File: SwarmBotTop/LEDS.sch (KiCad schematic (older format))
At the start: 8 parts, among them IC2 PCA9532BS,118

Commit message: Camera routing with all sensors and motors
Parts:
- C21: value C -> 1uF
- IC2: symbol PCA9532BS_118:PCA9532BS,118 -> SwarmBot-rescue:PCA9532BS,118-PCA9532BS_118
- R17, R18, R19: value R -> 330R
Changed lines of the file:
@@
 $EndComp
 $Comp
-L PCA9532BS_118:PCA9532BS,118 IC2
+L SwarmBot-rescue:PCA9532BS,118-PCA9532BS_118 IC2
 U 1 1 5DED59B9
 P 1500 1900
+AR Path="/5DED59B9" Ref="IC2"  Part="1"
+AR Path="/5DAF9EB1/5DED0A15/5DED59B9" Ref="IC2"  Part="1"
 F 0 "IC2" H 3150 1550 50  0000 L CNN
 F 1 "PCA9532BS,118" H 2950 1450 50  0000 L CNN
@@
 P 7950 3000
 F 0 "R17" V 7743 3000 50  0000 C CNN
-F 1 "R" V 7834 3000 50  0000 C CNN
+F 1 "330R" V 7834 3000 50  0000 C CNN
 F 2 "Resistor_SMD:R_0402_1005Metric" V 7880 3000 50  0001 C CNN
 F 3 "~" H 7950 3000 50  0001 C CNN
@@
 P 7950 3950
 F 0 "R18" V 7743 3950 50  0000 C CNN
-F 1 "R" V 7834 3950 50  0000 C CNN
+F 1 "330R" V 7834 3950 50  0000 C CNN
 F 2 "Resistor_SMD:R_0402_1005Metric" V 7880 3950 50  0001 C CNN
 F 3 "~" H 7950 3950 50  0001 C CNN
@@
 P 7950 4850
 F 0 "R19" V 7743 4850 50  0000 C CNN
-F 1 "R" V 7834 4850 50  0000 C CNN
+F 1 "330R" V 7834 4850 50  0000 C CNN
 F 2 "Resistor_SMD:R_0402_1005Metric" V 7880 4850 50  0001 C CNN
 F 3 "~" H 7950 4850 50  0001 C CNN
@@
 P 2600 800
 F 0 "C21" H 2715 846 50  0000 L CNN
-F 1 "C" H 2715 755 50  0000 L CNN
+F 1 "1uF" H 2715 755 50  0000 L CNN
 F 2 "Capacitor_SMD:C_0402_1005Metric" H 2638 650 50  0001 C CNN
 F 3 "~" H 2600 800 50  0001 C CNN

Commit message: V1 ready to order
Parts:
- removed D1, D2, D3: LED_BGRA, LED_SMD:LED_Kingbright_AAA3528ESGCT, symbol Device:LED_BGRA
- added D1, D2, D3: LED_ARGB, LED_SMD:LED_SK6812_EC15_1.5x1.5mm, symbol Device:LED_ARGB
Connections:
- net L0: now also D1.2 (RK)
- net L1: now also D1.3 (GK)
- net L2: now also D1.4 (BK)
- net L3: now also D2.4 (BK)
- net L4: now also D2.3 (GK)
- net L5: now also D2.2 (RK)
- net L6: now also D3.4 (BK)
- net L7: now also D3.2 (RK)
- net L8: now also D3.3 (GK)
- net at R17.1: now also D1.1 (A)
- net at R18.1: now also D2.1 (A)
- net at R19.1: now also D3.1 (A)
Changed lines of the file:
@@
 $EndDescr
-$Comp
-L Device:LED_BGRA D1
-U 1 1 5DED12E1
-P 8300 3000
-F 0 "D1" H 8300 2533 50  0000 C CNN
-F 1 "LED_BGRA" H 8300 2624 50  0000 C CNN
-F 2 "LED_SMD:LED_Kingbright_AAA3528ESGCT" H 8300 2950 50  0001 C CNN
-F 3 "~" H 8300 2950 50  0001 C CNN
-	1    8300 3000
-	-1   0    0    1
-$EndComp
-$Comp
-L Device:LED_BGRA D2
-U 1 1 5DED1B7E
-P 8300 3950
-F 0 "D2" H 8300 3483 50  0000 C CNN
-F 1 "LED_BGRA" H 8300 3574 50  0000 C CNN
-F 2 "LED_SMD:LED_Kingbright_AAA3528ESGCT" H 8300 3900 50  0001 C CNN
-F 3 "~" H 8300 3900 50  0001 C CNN
-	1    8300 3950
-	-1   0    0    1
-$EndComp
-$Comp
-L Device:LED_BGRA D3
-U 1 1 5DED2600
-P 8300 4850
-F 0 "D3" H 8300 4383 50  0000 C CNN
-F 1 "LED_BGRA" H 8300 4474 50  0000 C CNN
-F 2 "LED_SMD:LED_Kingbright_AAA3528ESGCT" H 8300 4800 50  0001 C CNN
-F 3 "~" H 8300 4800 50  0001 C CNN
-	1    8300 4850
-	-1   0    0    1
-$EndComp
 $Comp
 L SwarmBot-rescue:PCA9532BS,118-PCA9532BS_118 IC2
@@
 	-1   0    0    1
 $EndComp
-Text Label 8500 2800 0    50   ~ 0
+Text Label 8500 3200 0    50   ~ 0
 L0
 Text Label 8500 3000 0    50   ~ 0
 L1
-Text Label 8500 3200 0    50   ~ 0
+Text Label 8500 2800 0    50   ~ 0
 L2
 Text Label 8500 3750 0    50   ~ 0
@@
 Text Label 8500 4650 0    50   ~ 0
 L6
+Text Label 8500 5050 0    50   ~ 0
+L7
 Text Label 8500 4850 0    50   ~ 0
-L7
-Text Label 8500 5050 0    50   ~ 0
 L8
+$Comp
+L Device:LED_ARGB D3
+U 1 1 5E048630
+P 8300 4850
+F 0 "D3" H 8300 4383 50  0000 C CNN
+F 1 "LED_ARGB" H 8300 4474 50  0000 C CNN
+F 2 "LED_SMD:LED_SK6812_EC15_1.5x1.5mm" H 8300 4800 50  0001 C CNN
+F 3 "~" H 8300 4800 50  0001 C CNN
+	1    8300 4850
+	-1   0    0    1
+$EndComp
+$Comp
+L Device:LED_ARGB D2
+U 1 1 5E04ABFF
+P 8300 3950
+F 0 "D2" H 8300 3483 50  0000 C CNN
+F 1 "LED_ARGB" H 8300 3574 50  0000 C CNN
+F 2 "LED_SMD:LED_SK6812_EC15_1.5x1.5mm" H 8300 3900 50  0001 C CNN
+F 3 "~" H 8300 3900 50  0001 C CNN
+	1    8300 3950
+	-1   0    0    1
+$EndComp
+$Comp
+L Device:LED_ARGB D1
+U 1 1 5E04B11A
+P 8300 3000
+F 0 "D1" H 8300 2533 50  0000 C CNN
+F 1 "LED_ARGB" H 8300 2624 50  0000 C CNN
+F 2 "LED_SMD:LED_SK6812_EC15_1.5x1.5mm" H 8300 2950 50  0001 C CNN
+F 3 "~" H 8300 2950 50  0001 C CNN
+	1    8300 3000
+	-1   0    0    1
+$EndComp
 $EndSCHEMATC

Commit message: Final Design
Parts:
- added C6: 1uF, Capacitor_SMD:C_0402_1005Metric, symbol Device:C
- added D6, D7, D8: LED_ARGB, LED_SMD:LED_SK6812_EC15_1.5x1.5mm, symbol Device:LED_ARGB
- added IC1: PCA9532BS,118, Package_DFN_QFN:VQFN-24-1EP_4x4mm_P0.5mm_EP2.45x2.45mm, symbol SwarmBot-rescue:PCA9532BS,118-PCA9532BS_118
- added R10, R4, R7: 330R, Resistor_SMD:R_0402_1005Metric, symbol Device:R
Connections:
- net +3V3: now also C6.1, IC1.18, IC1.21, IC1.23, R10.2, R4.2, R7.2
- net GND: now also C6.2, IC1.22, IC1.24, IC1.25, IC1.9
- net L0: now also IC2.4; no longer IC2.1
- net L1: now also IC2.5; no longer IC2.3
- net L2: now also IC2.6; no longer IC2.2
- net L3: now also IC2.15; no longer IC2.17
- net L5: now also IC2.17; no longer IC2.15
- net L6: now also IC2.12; no longer IC2.7
- net L7: now also IC2.14; no longer IC2.10
- net L8: now also IC2.13; no longer IC2.8
- net SCL: now also IC1.19
- net SDA: now also IC1.20
- net PENDIR: now reaches IC2.11
- new net: D6.1 (A), R4.1
- new net: D7.1 (A), R7.1
- new net: D8.1 (A), R10.1
- new net CURRSET: IC2.7
- new net L10: D6.3 (GK), IC1.12
- new net L11: D6.2 (RK), IC1.13
- new net L12: D7.4 (BK), IC1.17
- new net L13: D7.3 (GK), IC1.16
- new net L14: D7.2 (RK), IC1.15
- new net L15: D8.4 (BK), IC1.7
- new net L16: D8.3 (GK), IC1.8
- new net L17: D8.2 (RK), IC1.10
- new net L9: D6.4 (BK), IC1.11
- new net PENSTEP: IC2.10
- new net STEPPEREN: IC2.8
- no-connect marks 4 -> 0

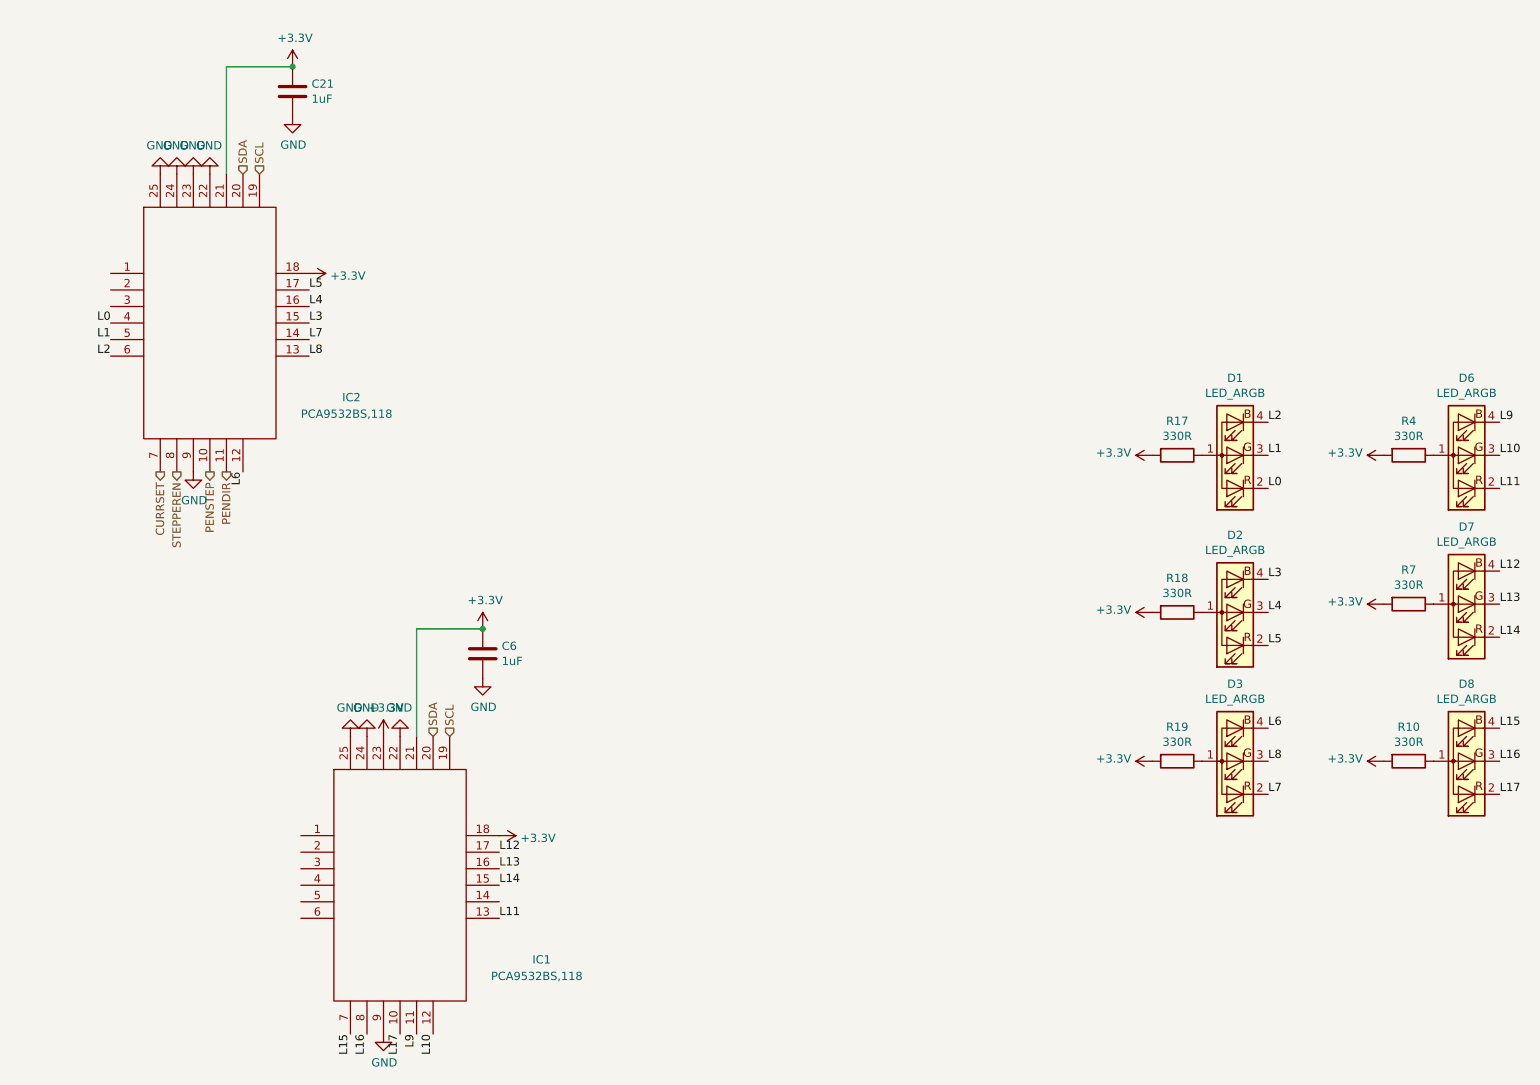
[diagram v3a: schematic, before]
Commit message: Updated LED drivers
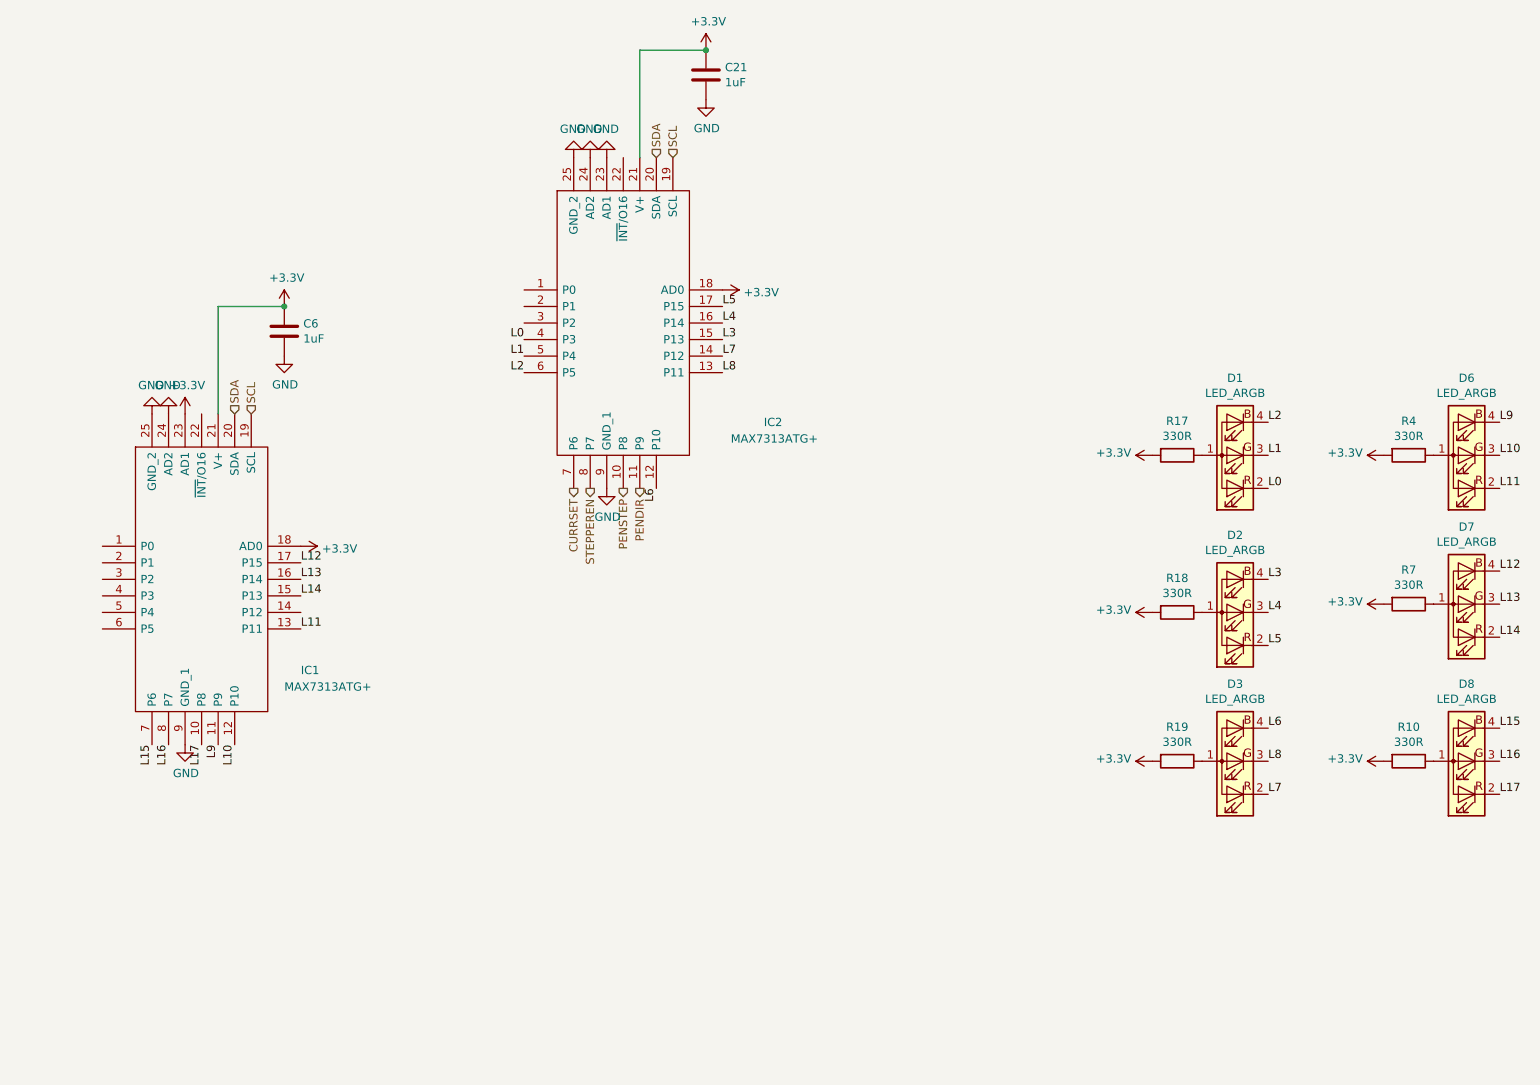
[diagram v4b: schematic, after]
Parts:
- removed IC1, IC2: PCA9532BS,118, Package_DFN_QFN:VQFN-24-1EP_4x4mm_P0.5mm_EP2.45x2.45mm, symbol SwarmBot-rescue:PCA9532BS,118-PCA9532BS_118
- added IC1, IC2: MAX7313ATG+, MAX7313ATG+:QFN50P400X400X80-25N, symbol MAX7313ATG+:MAX7313ATG+
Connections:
- net +3V3: now also IC1.18 (AD0), IC1.21 (V+), IC1.23 (AD1), IC2.18 (AD0), IC2.21 (V+)
- net CURRSET: now also IC2.7 (P6)
- net GND: now also IC1.24 (AD2), IC1.25 (GND_2), IC1.9 (GND_1), IC2.23 (AD1), IC2.24 (AD2), IC2.25 (GND_2), IC2.9 (GND_1)
- net L0: now also IC2.4 (P3)
- net L1: now also IC2.5 (P4)
- net L10: now also IC1.12 (P10)
- net L11: now also IC1.13 (P11)
- net L12: now also IC1.17 (P15)
- net L13: now also IC1.16 (P14)
- net L14: now also IC1.15 (P13)
- net L15: now also IC1.7 (P6)
- net L16: now also IC1.8 (P7)
- net L17: now also IC1.10 (P8)
- net L2: now also IC2.6 (P5)
- net L3: now also IC2.15 (P13)
- net L4: now also IC2.16 (P14)
- net L5: now also IC2.17 (P15)
- net L6: now also IC2.12 (P10)
- net L7: now also IC2.14 (P12)
- net L8: now also IC2.13 (P11)
- net L9: now also IC1.11 (P9)
- net PENDIR: now also IC2.11 (P9)
- net PENSTEP: now also IC2.10 (P8)
- net SCL: now also IC1.19 (SCL), IC2.19 (SCL)
- net SDA: now also IC1.20 (SDA), IC2.20 (SDA)
- net STEPPEREN: now also IC2.8 (P7)
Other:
- moved on the sheet: C21, C6
